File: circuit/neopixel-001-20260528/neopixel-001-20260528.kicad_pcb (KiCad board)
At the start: 2 copper layers, 114.3 x 114.3 mm, 67 parts, among them J1 Conn_NeoPixel, J2 Conn_01x02_Pin, J3 Conn_01x02_Pin, P1 ESP32C3_{1}, P10 unitV3, P11 unitV4, P12 unitV4, P2 ESP32C3_{1}, P3 ESP32C3_{2}, P4 ESP32C3_{2}, P5 unitV1, P6 unitV1, P7 unitV2, P8 unitV2, P9 unitV3, SW1 SW_SPST_LED, SW2 SW_SPST_LED, SW3 SW_SPST_LED, SW4 SW_SPST_LED, U1 SSD1306, U2 Aexit_0-50_Voltmeter

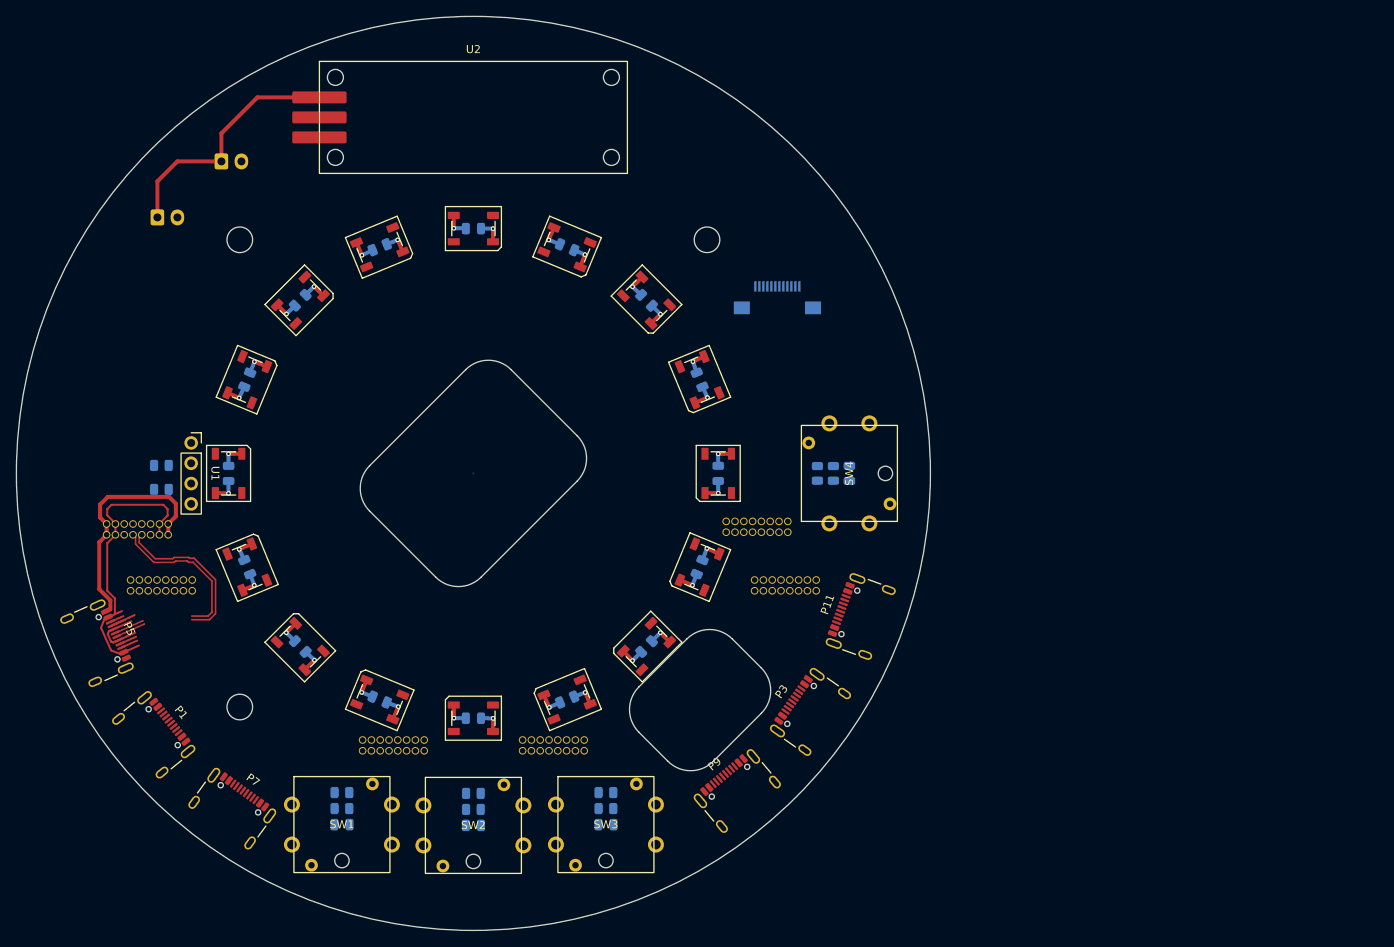
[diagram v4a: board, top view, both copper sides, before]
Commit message: Update ネオピクセル基板のPCBを進めた
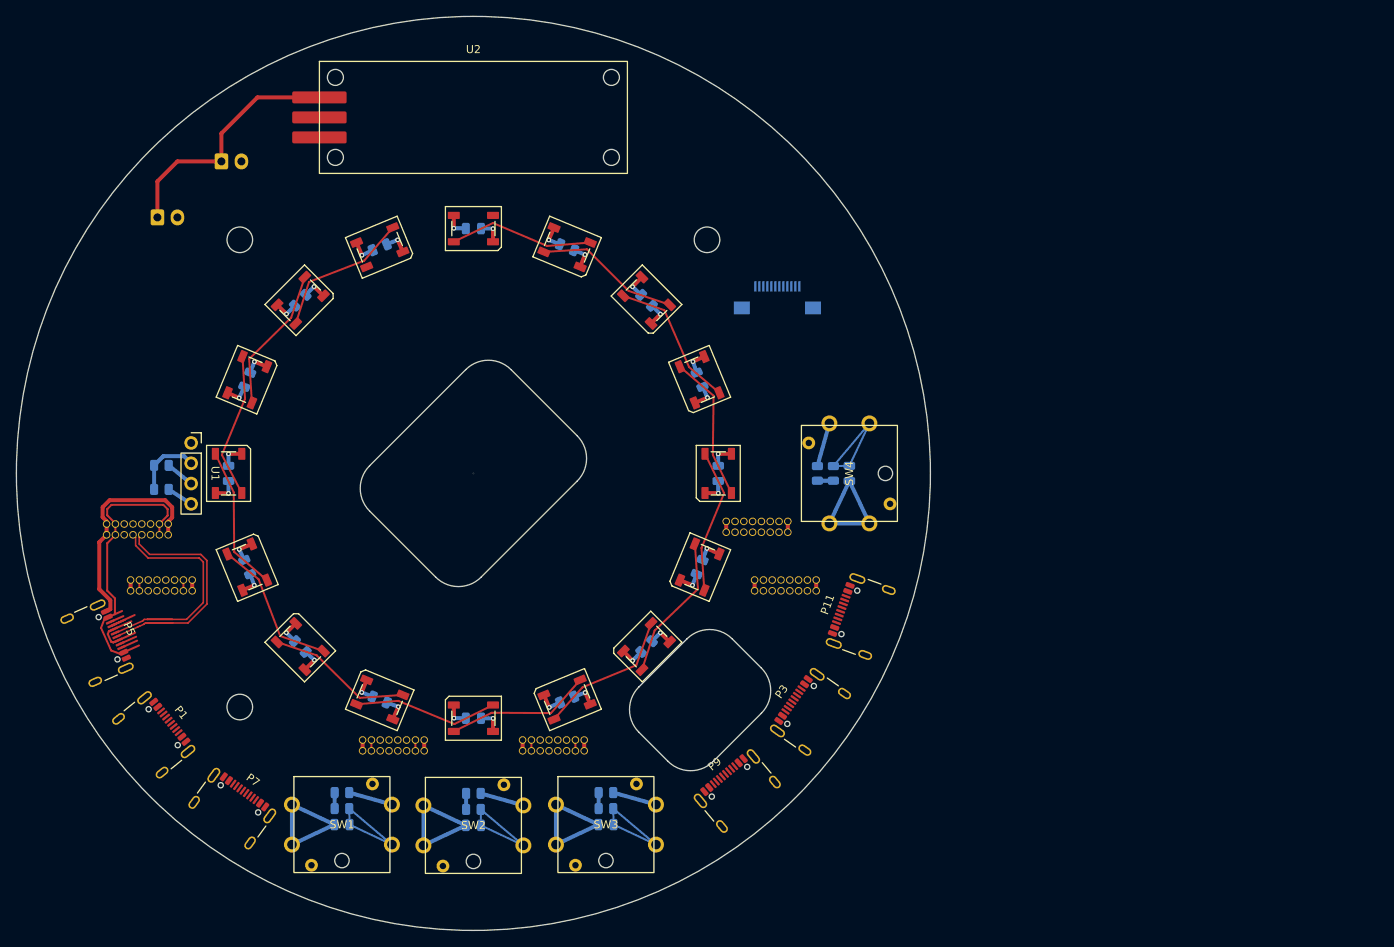
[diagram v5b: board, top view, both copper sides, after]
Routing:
- net GND: track 80.1 -> 158.6 mm
- net Net-(D11-DOUT): track 0.00 -> 18.3 mm
- net Net-(D15-DOUT): track 0.00 -> 18.3 mm
- net Net-(D6-DOUT): track 0.00 -> 18.3 mm
- net Net-(D4-DOUT): track 0.00 -> 18.3 mm
- net Net-(D13-DOUT): track 0.00 -> 18.2 mm
- net Net-(D8-DOUT): track 0.00 -> 18.2 mm
- net Net-(D14-DOUT): track 0.00 -> 18.2 mm
- net Net-(D10-DIN): track 0.00 -> 18.2 mm
- net Net-(D10-DOUT): track 0.00 -> 18.2 mm
- net Net-(D1-DOUT): track 0.00 -> 18.2 mm
- net Net-(D12-DOUT): track 0.00 -> 18.2 mm
- net Net-(D5-DOUT): track 0.00 -> 18.2 mm
- net Net-(D7-DOUT): track 0.00 -> 18.2 mm
- net Net-(D2-DOUT): track 0.00 -> 18.2 mm
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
